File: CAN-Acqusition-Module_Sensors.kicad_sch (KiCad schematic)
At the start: 22 parts, among them U7 SCD30, U8 SHT35-DIS

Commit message: Added as-ordered P/Ns and regenerated Gerbers
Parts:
- D19, D20: Mfr. (none) -> Diodes Incorporated; P/N (none) -> D1213A-01SO-7
- R38, R43, R47, R48: Mfr. (none) -> Stackpole; P/N (none) -> RMCF0603ZT0R00
- R39: Mfr. (none) -> Stackpole; P/N (none) -> RMCF0603FT10K0
- R50, R51: Mfr. (none) -> Stackpole; P/N (none) -> RMCF0603FT1K00
- U7: Mfr. (none) -> Sensirion; P/N (none) -> SCD30
- U8: Mfr. (none) -> Sensirion; P/N (none) -> SHT35-DIS-B10KS
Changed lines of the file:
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@@
+      (effects (font (size 1.27 1.27)) hide)
+    )
+    (property "Mfr." "Diodes Incorporated" (id 4) (at 118.11 107.95 0)
+      (effects (font (size 1.27 1.27)) hide)
+    )
+    (property "P/N" "D1213A-01SO-7" (id 5) (at 118.11 107.95 0)
       (effects (font (size 1.27 1.27)) hide)
     )
@@
       (effects (font (size 1.27 1.27)) hide)
     )
+    (property "Mfr." "Diodes Incorporated" (id 4) (at 104.14 107.95 0)
+      (effects (font (size 1.27 1.27)) hide)
+    )
+    (property "P/N" "D1213A-01SO-7" (id 5) (at 104.14 107.95 0)
+      (effects (font (size 1.27 1.27)) hide)
+    )
     (pin "1")
     (pin "2")
@@
       (effects (font (size 1.27 1.27)) hide)
     )
+    (property "Mfr." "Stackpole" (id 4) (at 163.83 123.19 0)
+      (effects (font (size 1.27 1.27)) hide)
+    )
+    (property "P/N" "RMCF0603ZT0R00" (id 5) (at 163.83 123.19 0)
+      (effects (font (size 1.27 1.27)) hide)
+    )
     (pin "1")
     (pin "2")
@@
       (effects (font (size 1.27 1.27)) hide)
     )
+    (property "Mfr." "Stackpole" (id 4) (at 149.86 120.65 0)
+      (effects (font (size 1.27 1.27)) hide)
+    )
+    (property "P/N" "RMCF0603ZT0R00" (id 5) (at 149.86 120.65 0)
+      (effects (font (size 1.27 1.27)) hide)
+    )
     (pin "1")
     (pin "2")
@@
     )
     (property "Datasheet" "https://sensirion.com/media/documents/4EAF6AF8/61652C3C/Sensirion_CO2_Sensors_SCD30_Datasheet.pdf" (id 3) (at 91.44 137.16 0)
+      (effects (font (size 1.27 1.27)) hide)
+    )
+    (property "Mfr." "Sensirion" (id 4) (at 74.93 113.03 0)
+      (effects (font (size 1.27 1.27)) hide)
+    )
+    (property "P/N" "SCD30" (id 5) (at 74.93 113.03 0)
       (effects (font (size 1.27 1.27)) hide)
     )
@@
       (effects (font (size 1.27 1.27)) hide)
     )
+    (property "Mfr." "Stackpole" (id 4) (at 205.74 62.23 0)
+      (effects (font (size 1.27 1.27)) hide)
+    )
+    (property "P/N" "RMCF0603FT1K00" (id 5) (at 205.74 62.23 0)
+      (effects (font (size 1.27 1.27)) hide)
+    )
     (pin "1")
     (pin "2")
@@
       (effects (font (size 1.27 1.27)) hide)
     )
+    (property "Mfr." "Stackpole" (id 4) (at 76.2 38.1 0)
+      (effects (font (size 1.27 1.27)) hide)
+    )
+    (property "P/N" "RMCF0603ZT0R00" (id 5) (at 76.2 38.1 0)
+      (effects (font (size 1.27 1.27)) hide)
+    )
     (pin "1")
     (pin "2")
@@
     )
     (property "Datasheet" "https://www.sensirion.com/fileadmin/user_upload/customers/sensirion/Dokumente/2_Humidity_Sensors/Datasheets/Sensirion_Humidity_Sensors_SHT3x_Datasheet_digital.pdf" (id 3) (at 109.22 33.02 0)
+      (effects (font (size 1.27 1.27)) hide)
+    )
+    (property "Mfr." "Sensirion" (id 4) (at 109.22 34.29 0)
+      (effects (font (size 1.27 1.27)) hide)
+    )
+    (property "P/N" "SHT35-DIS-B10KS" (id 5) (at 109.22 34.29 0)
       (effects (font (size 1.27 1.27)) hide)
     )
@@
       (effects (font (size 1.27 1.27)) hide)
     )
+    (property "Mfr." "Stackpole" (id 4) (at 219.71 62.23 0)
+      (effects (font (size 1.27 1.27)) hide)
+    )
+    (property "P/N" "RMCF0603FT1K00" (id 5) (at 219.71 62.23 0)
+      (effects (font (size 1.27 1.27)) hide)
+    )
     (pin "1")
     (pin "2")
@@
       (effects (font (size 1.27 1.27)) hide)
     )
+    (property "Mfr." "Stackpole" (id 4) (at 88.9 27.94 0)
+      (effects (font (size 1.27 1.27)) hide)
+    )
+    (property "P/N" "RMCF0603FT10K0" (id 5) (at 88.9 27.94 0)
+      (effects (font (size 1.27 1.27)) hide)
+    )
     (pin "1")
     (pin "2")
@@
       (effects (font (size 1.27 1.27)) hide)
     )
+    (property "Mfr." "Stackpole" (id 4) (at 111.76 149.86 0)
+      (effects (font (size 1.27 1.27)) hide)
+    )
+    (property "P/N" "RMCF0603ZT0R00" (id 5) (at 111.76 149.86 0)
+      (effects (font (size 1.27 1.27)) hide)
+    )

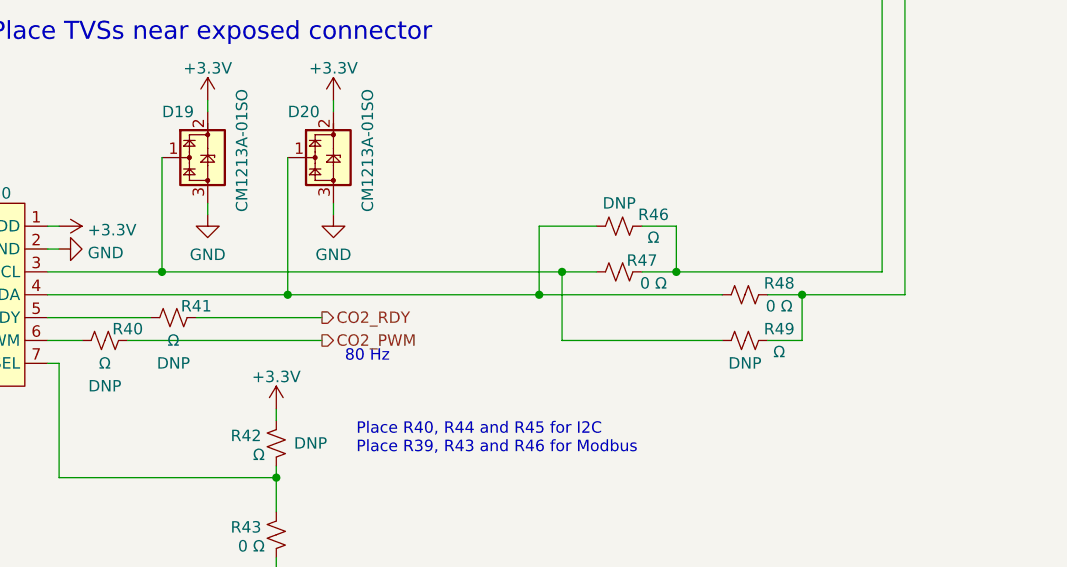
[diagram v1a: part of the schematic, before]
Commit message: Rev.A2 pretty much finished
V USB bypasses inductor L2
Srew terminal pin holes size reduced
Thermally isolated SHT3x
Fixed U1 footprint
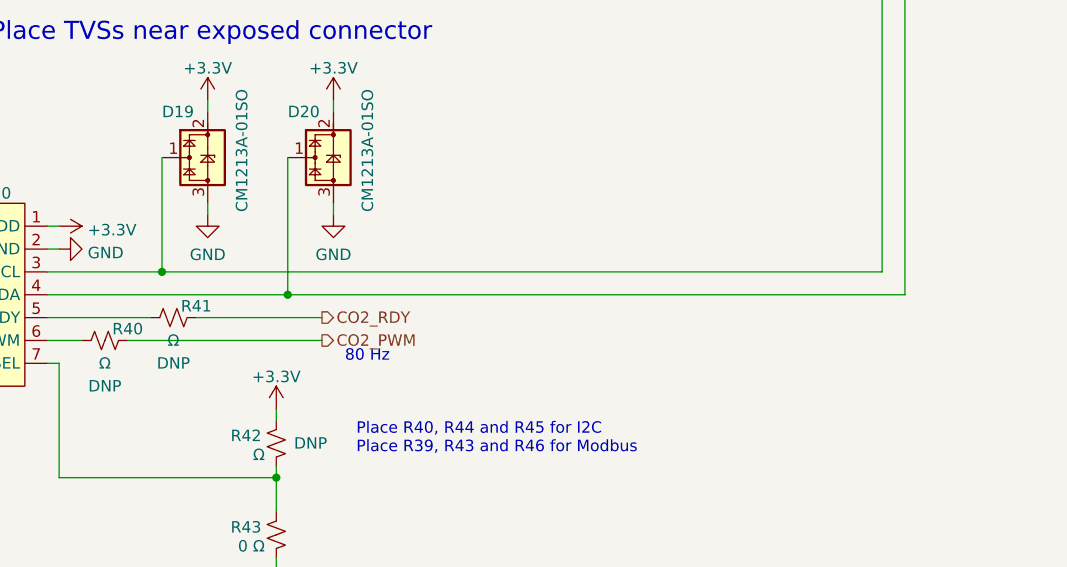
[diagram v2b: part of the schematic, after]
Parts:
- removed R46, R49: Ω, Resistor_SMD:R_0603_1608Metric, symbol Device:R_Small_US
- removed R47, R48: 0 Ω, Resistor_SMD:R_0603_1608Metric, symbol Device:R_Small_US
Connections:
- net I2C_SCL: now also D19.1 (CH1), U7.3 (TX/SCL)
- net I2C_SDA: now also D20.1 (CH1), U7.4 (RX/SDA)
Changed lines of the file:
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@@
   (junction (at 88.9 34.29) (diameter 0) (color 0 0 0 0)
   )
-  (junction (at 170.18 123.19) (diameter 0) (color 0 0 0 0)
-  )
-  (junction (at 140.97 123.19) (diameter 0) (color 0 0 0 0)
-  )
   (junction (at 205.74 71.12) (diameter 0) (color 0 0 0 0)
   )
   (junction (at 76.2 31.75) (diameter 0) (color 0 0 0 0)
   )
-  (junction (at 143.51 120.65) (diameter 0) (color 0 0 0 0)
-  )
   (junction (at 111.76 143.51) (diameter 0) (color 0 0 0 0)
   )
@@
   (junction (at 99.06 120.65) (diameter 0) (color 0 0 0 0)
   )
-  (junction (at 156.21 120.65) (diameter 0) (color 0 0 0 0)
-  )
   (wire (pts (xy 118.11 101.6) (xy 118.11 102.87))
     (stroke (width 0) (type default) (color 0 0 0 0))
@@
     (stroke (width 0) (type default) (color 0 0 0 0))
   )
-  (wire (pts (xy 113.03 123.19) (xy 140.97 123.19))
+  (wire (pts (xy 113.03 123.19) (xy 181.61 123.19))
     (stroke (width 0) (type default) (color 0 0 0 0))
   )
@@
     (stroke (width 0) (type default) (color 0 0 0 0))
   )
-  (wire (pts (xy 143.51 120.65) (xy 147.32 120.65))
+  (wire (pts (xy 99.06 120.65) (xy 179.07 120.65))
     (stroke (width 0) (type default) (color 0 0 0 0))
   )
@@
     (stroke (width 0) (type default) (color 0 0 0 0))
   )
-  (wire (pts (xy 170.18 123.19) (xy 181.61 123.19))
-    (stroke (width 0) (type default) (color 0 0 0 0))
-  )
-  (wire (pts (xy 99.06 120.65) (xy 143.51 120.65))
-    (stroke (width 0) (type default) (color 0 0 0 0))
-  )
-  (wire (pts (xy 166.37 128.27) (xy 170.18 128.27))
-    (stroke (width 0) (type default) (color 0 0 0 0))
-  )
   (wire (pts (xy 102.87 125.73) (xy 116.84 125.73))
     (stroke (width 0) (type default) (color 0 0 0 0))
@@
     (stroke (width 0) (type default) (color 0 0 0 0))
   )
-  (wire (pts (xy 156.21 120.65) (xy 179.07 120.65))
-    (stroke (width 0) (type default) (color 0 0 0 0))
-  )
-  (wire (pts (xy 156.21 120.65) (xy 156.21 115.57))
-    (stroke (width 0) (type default) (color 0 0 0 0))
-  )
   (wire (pts (xy 55.88 127) (xy 55.88 124.46))
     (stroke (width 0) (type default) (color 0 0 0 0))
@@
     (stroke (width 0) (type default) (color 0 0 0 0))
   )
-  (wire (pts (xy 143.51 128.27) (xy 143.51 120.65))
-    (stroke (width 0) (type default) (color 0 0 0 0))
-  )
   (wire (pts (xy 46.99 127) (xy 55.88 127))
     (stroke (width 0) (type default) (color 0 0 0 0))
   )
-  (wire (pts (xy 140.97 115.57) (xy 140.97 123.19))
-    (stroke (width 0) (type default) (color 0 0 0 0))
-  )
   (wire (pts (xy 219.71 68.58) (xy 228.6 68.58))
     (stroke (width 0) (type default) (color 0 0 0 0))
@@
     (stroke (width 0) (type default) (color 0 0 0 0))
   )
-  (wire (pts (xy 166.37 123.19) (xy 170.18 123.19))
-    (stroke (width 0) (type default) (color 0 0 0 0))
-  )
   (wire (pts (xy 219.71 64.77) (xy 219.71 68.58))
     (stroke (width 0) (type default) (color 0 0 0 0))
@@
     (stroke (width 0) (type default) (color 0 0 0 0))
   )
-  (wire (pts (xy 161.29 128.27) (xy 143.51 128.27))
-    (stroke (width 0) (type default) (color 0 0 0 0))
-  )
   (wire (pts (xy 55.88 119.38) (xy 55.88 116.84))
     (stroke (width 0) (type default) (color 0 0 0 0))
@@
     (stroke (width 0) (type default) (color 0 0 0 0))
   )
-  (wire (pts (xy 147.32 115.57) (xy 140.97 115.57))
-    (stroke (width 0) (type default) (color 0 0 0 0))
-  )
-  (wire (pts (xy 170.18 128.27) (xy 170.18 123.19))
-    (stroke (width 0) (type default) (color 0 0 0 0))
-  )
-  (wire (pts (xy 156.21 115.57) (xy 152.4 115.57))
-    (stroke (width 0) (type default) (color 0 0 0 0))
-  )
   (wire (pts (xy 111.76 142.24) (xy 111.76 143.51))
     (stroke (width 0) (type default) (color 0 0 0 0))
@@
     (stroke (width 0) (type default) (color 0 0 0 0))
   )
-  (wire (pts (xy 152.4 120.65) (xy 156.21 120.65))
-    (stroke (width 0) (type default) (color 0 0 0 0))
-  )
   (wire (pts (xy 113.03 107.95) (xy 113.03 123.19))
-    (stroke (width 0) (type default) (color 0 0 0 0))
-  )
-  (wire (pts (xy 140.97 123.19) (xy 161.29 123.19))
     (stroke (width 0) (type default) (color 0 0 0 0))
   )
@@
     (pin "2")
     (pin "3")
-  )
-  (symbol (lib_id "Device:R_Small_US") (at 163.83 123.19 90) (unit 1)
-    (in_bom yes) (on_board yes)
-    (property "Reference" "R48" (id 0) (at 167.64 121.92 90))
-    (property "Value" "0 Ω" (id 1) (at 167.64 124.46 90))
-    (property "Footprint" "Resistor_SMD:R_0603_1608Metric" (id 2) (at 163.83 123.19 0)
-      (effects (font (size 1.27 1.27)) hide)
-    )
-    (property "Datasheet" "~" (id 3) (at 163.83 123.19 0)
-      (effects (font (size 1.27 1.27)) hide)
-    )
-    (property "Mfr." "Stackpole" (id 4) (at 163.83 123.19 0)
-      (effects (font (size 1.27 1.27)) hide)
-    )
-    (property "P/N" "RMCF0603ZT0R00" (id 5) (at 163.83 123.19 0)
-      (effects (font (size 1.27 1.27)) hide)
-    )
-    (pin "1")
-    (pin "2")
-  )
-  (symbol (lib_id "Device:R_Small_US") (at 149.86 120.65 90) (unit 1)
-    (in_bom yes) (on_board yes)
-    (property "Reference" "R47" (id 0) (at 152.4 119.38 90))
-    (property "Value" "0 Ω" (id 1) (at 153.67 121.92 90))
-    (property "Footprint" "Resistor_SMD:R_0603_1608Metric" (id 2) (at 149.86 120.65 0)
-      (effects (font (size 1.27 1.27)) hide)
-    )
-    (property "Datasheet" "~" (id 3) (at 149.86 120.65 0)
-      (effects (font (size 1.27 1.27)) hide)
-    )
-    (property "Mfr." "Stackpole" (id 4) (at 149.86 120.65 0)
-      (effects (font (size 1.27 1.27)) hide)
-    )
-    (property "P/N" "RMCF0603ZT0R00" (id 5) (at 149.86 120.65 0)
-      (effects (font (size 1.27 1.27)) hide)
-    )
-    (pin "1")
-    (pin "2")
   )
   (symbol (lib_id "CAN-Acquisition-Module:SCD30") (at 74.93 113.03 0) (unit 1)
@@
       (effects (font (size 1.27 1.27)) hide)
     )
-    (pin "1")
-    (pin "2")
-  )
-  (symbol (lib_id "Device:R_Small_US") (at 149.86 115.57 90) (unit 1)
-    (in_bom yes) (on_board yes)
-    (property "Reference" "R46" (id 0) (at 153.67 114.3 90))
-    (property "Value" "Ω" (id 1) (at 153.67 116.84 90))
-    (property "Footprint" "Resistor_SMD:R_0603_1608Metric" (id 2) (at 149.86 115.57 0)
-      (effects (font (size 1.27 1.27)) hide)
-    )
-    (property "Datasheet" "~" (id 3) (at 149.86 115.57 0)
-      (effects (font (size 1.27 1.27)) hide)
-    )
-    (property "Do Not Place" "DNP" (id 4) (at 149.86 113.03 90))
     (pin "1")
     (pin "2")
@@
     (pin "1")
     (pin "2")
-  )
-  (symbol (lib_id "Device:R_Small_US") (at 163.83 128.27 90) (unit 1)
-    (in_bom yes) (on_board yes)
-    (property "Reference" "R49" (id 0) (at 167.64 127 90))
-    (property "Value" "Ω" (id 1) (at 167.64 129.54 90))
-    (property "Footprint" "Resistor_SMD:R_0603_1608Metric" (id 2) (at 163.83 128.27 0)
-      (effects (font (size 1.27 1.27)) hide)
-    )
-    (property "Datasheet" "~" (id 3) (at 163.83 128.27 0)
-      (effects (font (size 1.27 1.27)) hide)
-    )
-    (property "Do Not Place" "DNP" (id 4) (at 163.83 130.81 90))
-    (pin "1")
-    (pin "2")

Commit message: BOM updated for LCSC. Still a WIP.
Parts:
- R37, R40, R41, R42, R44, R45: LCSC (none) -> DNP
- R38, R39, R43, R50, R51: Tolerance (none) -> 1%
- U7: Do Not Place (none) -> DNP; LCSC (none) -> DNP
- U8: LCSC (none) -> C90161
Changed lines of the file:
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@@
     )
     (property "Do Not Place" "DNP" (id 4) (at 92.71 133.3469 90))
+    (property "LCSC" "DNP" (id 5) (at 92.71 128.27 0)
+      (effects (font (size 1.27 1.27)) hide)
+    )
     (pin "1")
     (pin "2")
@@
     )
     (property "P/N" "SCD30" (id 5) (at 74.93 113.03 0)
+      (effects (font (size 1.27 1.27)) hide)
+    )
+    (property "Do Not Place" "DNP" (id 6) (at 74.93 113.03 0)
+      (effects (font (size 1.27 1.27)) hide)
+    )
+    (property "LCSC" "DNP" (id 7) (at 74.93 113.03 0)
       (effects (font (size 1.27 1.27)) hide)
     )
@@
     )
     (property "Do Not Place" "DNP" (id 4) (at 124.46 41.91 90))
+    (property "LCSC" "DNP" (id 5) (at 124.46 36.83 0)
+      (effects (font (size 1.27 1.27)) hide)
+    )
     (pin "1")
     (pin "2")
@@
       (effects (font (size 1.27 1.27)) hide)
     )
+    (property "Tolerance" "1%" (id 6) (at 205.74 62.23 0)
+      (effects (font (size 1.27 1.27)) hide)
+    )
     (pin "1")
     (pin "2")
@@
     )
     (property "Do Not Place" "DNP" (id 4) (at 72.39 27.94 0))
+    (property "LCSC" "DNP" (id 5) (at 76.2 27.94 0)
+      (effects (font (size 1.27 1.27)) hide)
+    )
     (pin "1")
     (pin "2")
@@
     )
     (property "Do Not Place" "DNP" (id 4) (at 100.33 130.81 90))
+    (property "LCSC" "DNP" (id 5) (at 100.33 125.73 0)
+      (effects (font (size 1.27 1.27)) hide)
+    )
     (pin "1")
     (pin "2")
@@
     )
     (property "Do Not Place" "DNP" (id 4) (at 115.57 139.7 0))
+    (property "LCSC" "DNP" (id 5) (at 111.76 139.7 0)
+      (effects (font (size 1.27 1.27)) hide)
+    )
     (pin "1")
     (pin "2")
@@
       (effects (font (size 1.27 1.27)) hide)
     )
+    (property "Tolerance" "1%" (id 6) (at 76.2 38.1 0)
+      (effects (font (size 1.27 1.27)) hide)
+    )
     (pin "1")
     (pin "2")
@@
     )
     (property "P/N" "SHT35-DIS-B10KS" (id 5) (at 109.22 34.29 0)
+      (effects (font (size 1.27 1.27)) hide)
+    )
+    (property "LCSC" "C90161" (id 6) (at 109.22 34.29 0)
       (effects (font (size 1.27 1.27)) hide)
     )
@@
       (effects (font (size 1.27 1.27)) hide)
     )
+    (property "Tolerance" "1%" (id 6) (at 219.71 62.23 0)
+      (effects (font (size 1.27 1.27)) hide)
+    )
     (pin "1")
     (pin "2")
@@
     )
     (property "Do Not Place" "DNP" (id 4) (at 124.46 59.6869 90))
+    (property "LCSC" "DNP" (id 5) (at 124.46 54.61 0)
+      (effects (font (size 1.27 1.27)) hide)
+    )
     (pin "1")
     (pin "2")
@@
     )
     (property "P/N" "RMCF0603FT10K0" (id 5) (at 88.9 27.94 0)
+      (effects (font (size 1.27 1.27)) hide)
+    )
+    (property "Tolerance" "1%" (id 6) (at 88.9 27.94 0)
       (effects (font (size 1.27 1.27)) hide)
     )
@@
       (effects (font (size 1.27 1.27)) hide)
     )
+    (property "Tolerance" "1%" (id 6) (at 111.76 149.86 0)
+      (effects (font (size 1.27 1.27)) hide)
+    )

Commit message: BOM updated for LCSC. Still a WIP
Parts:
- D19, D20: LCSC (none) -> C558429
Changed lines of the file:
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@@
+      (effects (font (size 1.27 1.27)) hide)
+    )
+    (property "LCSC" "C558429" (id 6) (at 118.11 107.95 0)
       (effects (font (size 1.27 1.27)) hide)
     )
@@
       (effects (font (size 1.27 1.27)) hide)
     )
+    (property "LCSC" "C558429" (id 6) (at 104.14 107.95 0)
+      (effects (font (size 1.27 1.27)) hide)
+    )

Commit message: Created Rev B1
Replaced buck regulator S-8581AA with AP63200 because of shortage
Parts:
- C48: LCSC P/N (none) -> C386019; LCSC Package (none) -> 0805; LCSC Specs (none) -> 10uF X7R 6.3V
- C49: LCSC P/N (none) -> C386079; LCSC Package (none) -> 0603; LCSC Specs (none) -> 1uF X7R 25V
- C50: LCSC P/N (none) -> C77014; LCSC Package (none) -> 0402; LCSC Specs (none) -> 100nF X7R 16V
- D19, D20: LCSC C558429 -> (none); LCSC P/N (none) -> C558429; LCSC Package (none) -> SOT-23; LCSC Specs (none) -> TPCM1213A-01SO
- R37, R40, R41, R42, R44, R45: LCSC DNP -> (none); LCSC P/N (none) -> DNP; LCSC Package (none) -> DNP; LCSC Specs (none) -> DNP
- R38, R43: LCSC P/N (none) -> C21189; LCSC Package (none) -> 0603; LCSC Specs (none) -> 0R
- R39: LCSC P/N (none) -> C98220; LCSC Package (none) -> 0603; LCSC Specs (none) -> 10K 1%
- R50, R51: LCSC P/N (none) -> C22548; LCSC Package (none) -> 0603; LCSC Specs (none) -> 1K 1%
- U7: Do Not Place DNP -> (none); LCSC DNP -> (none); LCSC P/N (none) -> DNP; LCSC Package (none) -> DNP; LCSC Specs (none) -> DNP
- U8: LCSC C90161 -> (none); LCSC P/N (none) -> DNP; LCSC Package (none) -> DNP; LCSC Specs (none) -> DNP
